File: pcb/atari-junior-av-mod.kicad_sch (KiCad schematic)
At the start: 19 parts

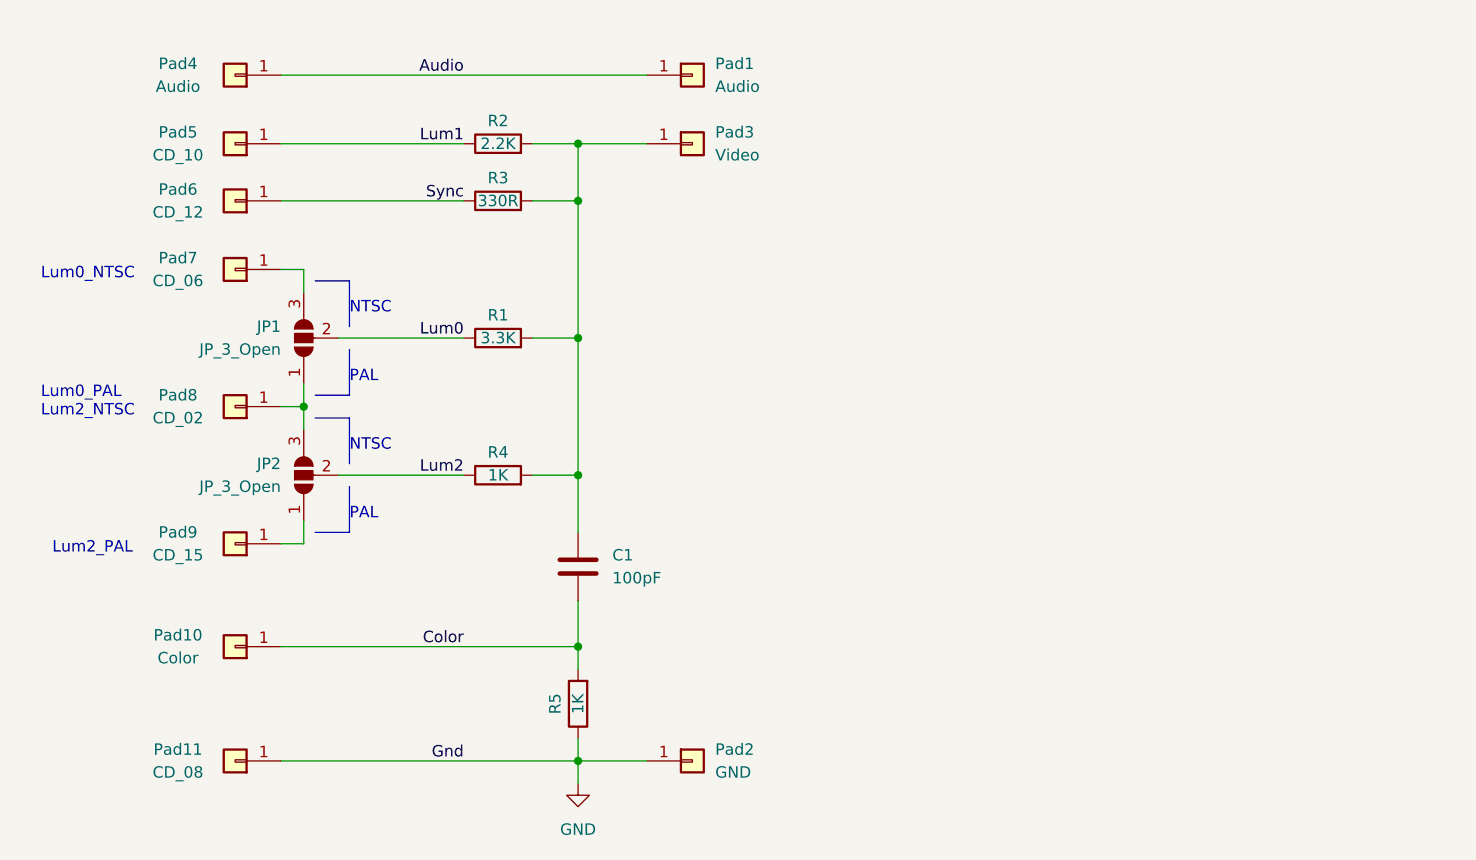
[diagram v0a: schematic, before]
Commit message: Beautify schematic and add mechanical footprints
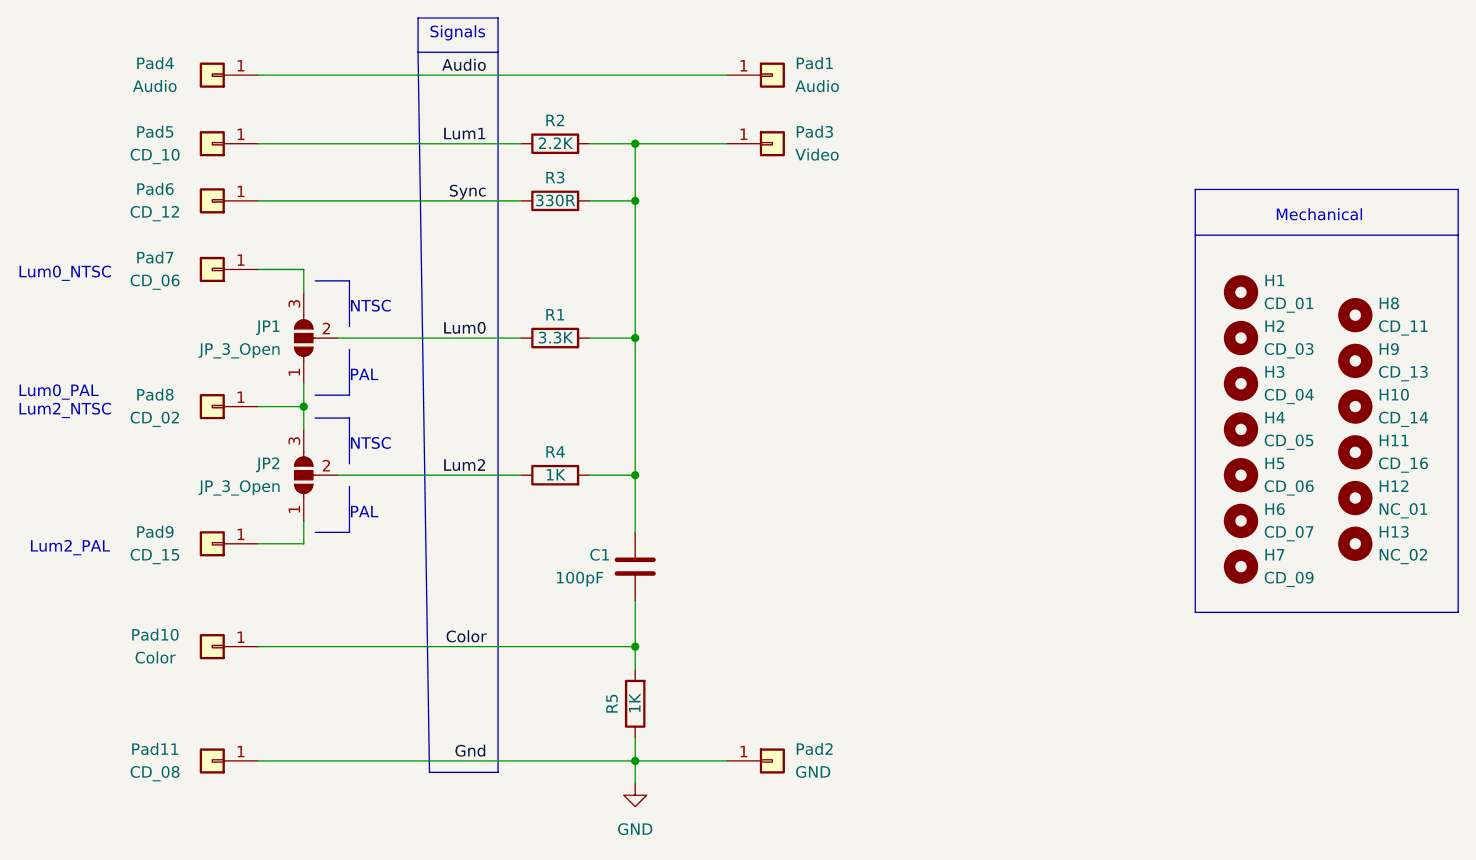
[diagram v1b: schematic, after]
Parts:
- added H1: CD_01, MeineBib:ModHole2mm, symbol Mechanical:MountingHole
- added H10: CD_14, MeineBib:ModHole2mm, symbol Mechanical:MountingHole
- added H11: CD_16, MeineBib:ModHole2mm, symbol Mechanical:MountingHole
- added H12: NC_01, MeineBib:ModHole2mm, symbol Mechanical:MountingHole
- added H13: NC_02, MeineBib:ModHole2mm, symbol Mechanical:MountingHole
- added H2: CD_03, MeineBib:ModHole2mm, symbol Mechanical:MountingHole
- added H3: CD_04, MeineBib:ModHole2mm, symbol Mechanical:MountingHole
- added H4: CD_05, MeineBib:ModHole2mm, symbol Mechanical:MountingHole
- added H5: CD_06, MeineBib:ModHole2mm, symbol Mechanical:MountingHole
- added H6: CD_07, MeineBib:ModHole2mm, symbol Mechanical:MountingHole
- added H7: CD_09, MeineBib:ModHole2mm, symbol Mechanical:MountingHole
- added H8: CD_11, MeineBib:ModHole2mm, symbol Mechanical:MountingHole
- added H9: CD_13, MeineBib:ModHole2mm, symbol Mechanical:MountingHole
- Pad1, Pad2, Pad3: footprint (none) -> MeineBib:ModWirePad
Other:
- note added: "Mechanical"
- note added: "Signals"
- company: (none) -> Binary-6
- title: (none) -> Atari junior AV mod
- moved on the sheet: C1, Pad1, Pad10, Pad11, Pad2, Pad3, Pad4, Pad5, Pad6, Pad7, Pad8, Pad9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
